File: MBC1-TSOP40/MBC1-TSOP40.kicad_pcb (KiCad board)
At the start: 2 copper layers, 13.5 x 23.3 mm, 4 parts

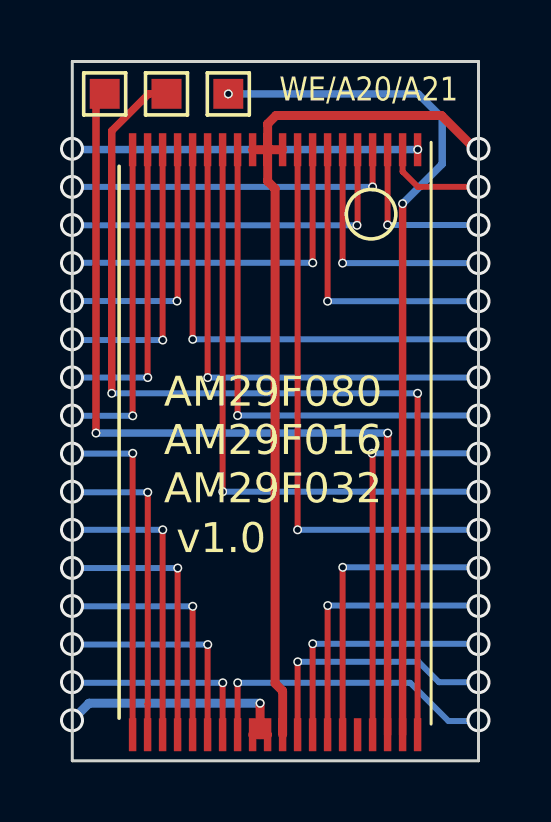
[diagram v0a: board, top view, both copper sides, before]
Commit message: Updated via size to reduce production costs
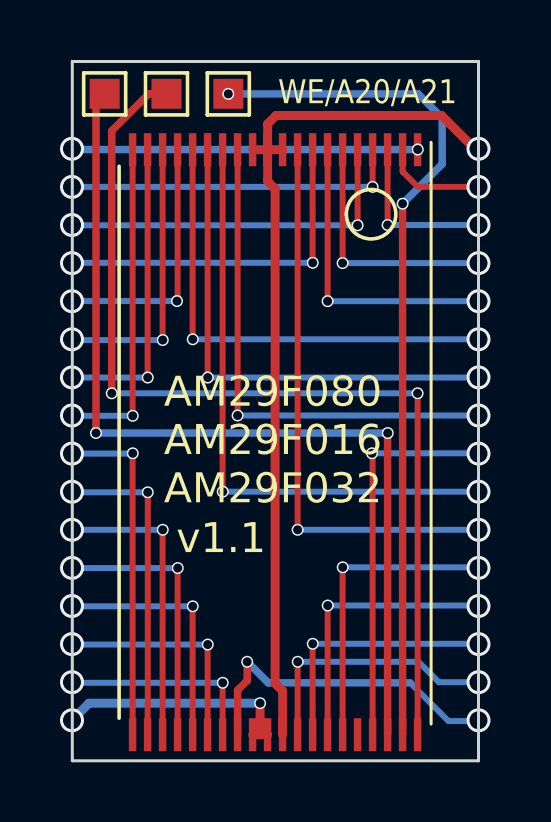
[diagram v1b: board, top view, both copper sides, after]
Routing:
- net D3: track 10.2 -> 11.0 mm
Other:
- board text added: "v1.1"
- board text removed: "v1.0"
